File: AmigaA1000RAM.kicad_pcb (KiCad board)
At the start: 4 copper layers, 104.1 x 55.9 mm, 42 parts, among them J1 Conn_02x04_Odd_Even, J2 Conn_02x04_Odd_Even, J3 Conn_02x04_Odd_Even, J4 Conn_02x04_Odd_Even, J5 Conn_02x04_Odd_Even, J6 Conn_02x04_Odd_Even, J7 Conn_02x04_Odd_Even, J8 Conn_02x04_Odd_Even, J9 Conn_01x03, U1 74AHCT00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

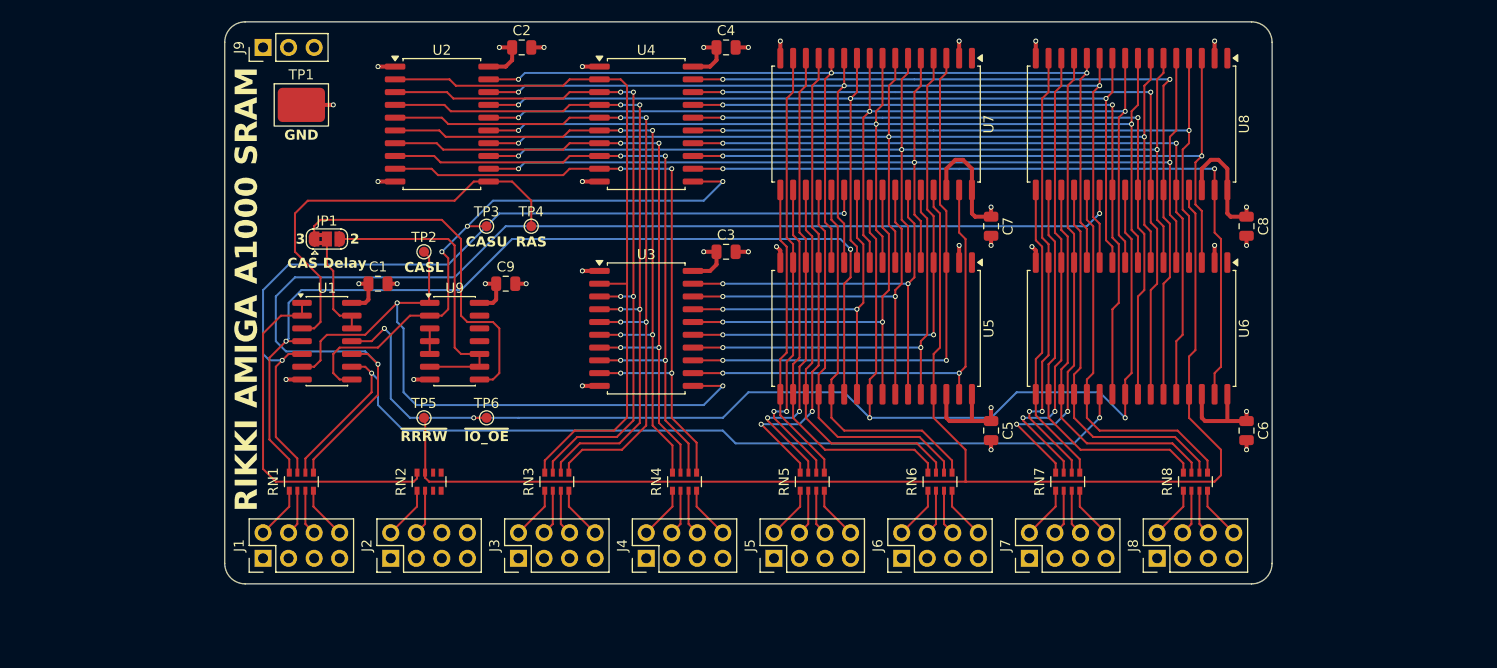
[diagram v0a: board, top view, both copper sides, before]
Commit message: Update PCB for card edge connector
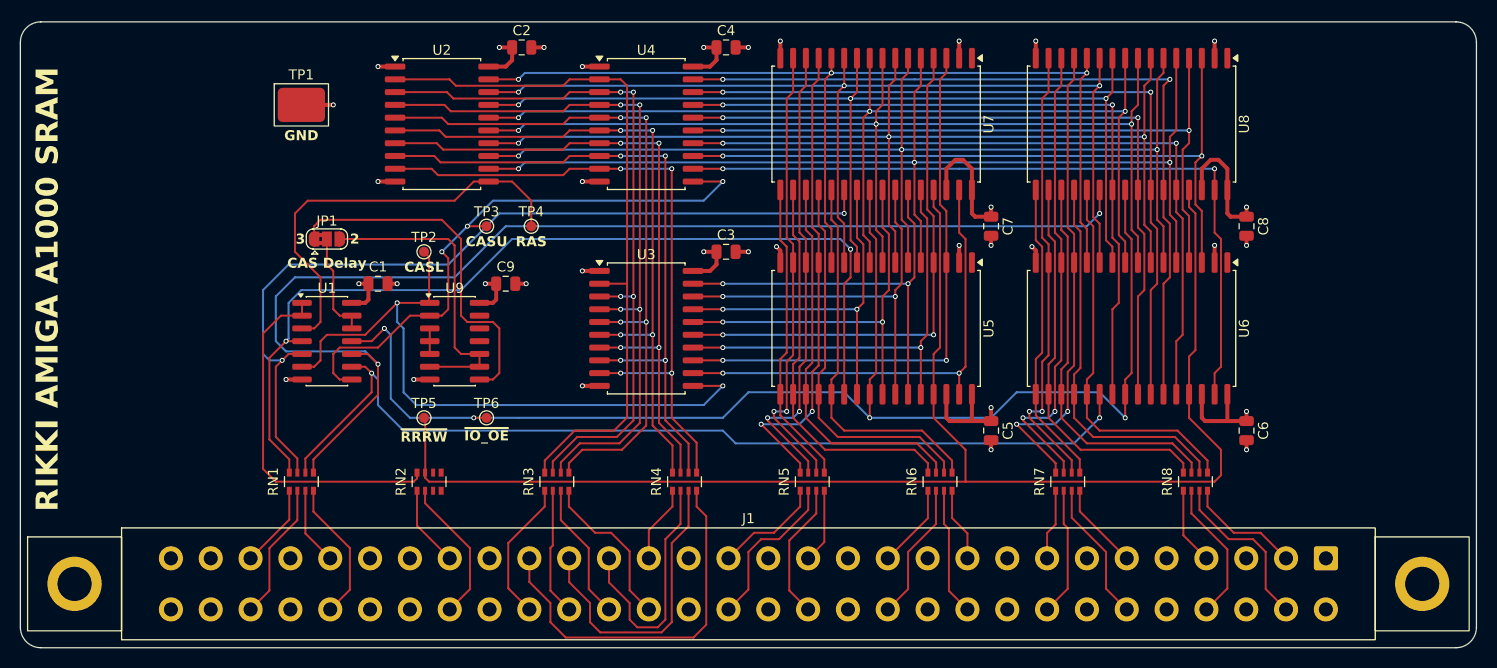
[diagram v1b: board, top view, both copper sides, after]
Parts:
- removed J2, J3, J4, J5, J6, J7, J8: Conn_02x04_Odd_Even, Connector_PinHeader_2.54mm:PinHeader_2x04_P2.54mm_Vertical
- removed J9: Conn_01x03, Connector_PinHeader_2.54mm:PinHeader_1x03_P2.54mm_Vertical
- J1: value Conn_02x04_Odd_Even -> Conn_02x30_Top_Bottom_Letter; footprint Connector_PinHeader_2.54mm:PinHeader_2x04_P2.54mm_Vertical -> AmigaA1000RAM:CardEdgeSocket_2x30_P3.96mm
- TP1: value GND -> TestPoint_Small
- TP2: value CASL -> TestPoint_Small
- TP3: value CASU -> TestPoint_Small
- TP4: value RAS -> TestPoint_Small
- TP5: value ~{RRRW} -> TestPoint_Small
- TP6: value ~{IO_OE} -> TestPoint_Small
- moved J1 48.3 mm to (139.7, 114.3), turned to 0 degrees
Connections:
- J1 pad 2: ~{XCASL0} -> XDRD15
- J1 pad 3: GND -> +5V
- J1 pad 4: ~{XCASL1} -> XDRD12
- J1 pad 6: ~{XCASU0} -> XDRD11
- J1 pad 7: GND -> +5V
- J1 pad 8: ~{XCASU1} -> XDRD8
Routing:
- net XDRA7: track 5.26 -> 37.6 mm
- net XDRA6: track 4.54 -> 29.9 mm
- net XDRA5: track 4.54 -> 24.6 mm
- net XDRD14: track 4.54 -> 16.8 mm
- net XDRD1: track 4.54 -> 16.1 mm
- net XDRA3: track 5.26 -> 16.0 mm
- net ~{XRRW}: track 4.54 -> 14.5 mm
- net XDRD13: track 4.54 -> 14.1 mm
- net XDRD10: track 4.54 -> 14.1 mm
- net XDRA2: track 4.54 -> 13.8 mm
- net XDRD5: track 4.54 -> 13.8 mm
- net ~{XCASL1}: track 4.54 -> 13.7 mm
- net XDRD2: track 4.54 -> 13.7 mm
- net XDRA0: track 5.26 -> 14.2 mm
- net ~{XCASU1}: track 5.26 -> 14.1 mm
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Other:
- board size 104.1 x 55.9 mm -> 144.8 x 62.2 mm
- board text added: "CASL"
- board text added: "CASU"
- board text added: "GND"
- board text added: "RAS"
- board text added: "~{IO_OE}"
- board text added: "~{RRRW}"
